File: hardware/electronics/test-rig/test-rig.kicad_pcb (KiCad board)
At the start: 2 copper layers, 154.8 x 27.9 mm, 57 parts, among them IC1 23LC1024, J1 JUMPER_OPEN, J2 JUMPER_CLOSED, J3 JUMPER_CLOSED, J4 AudioJack3_Switch, J5 Screw_Terminal_1x02, J6 Screw_Terminal_1x02, P1 CONN_01X15, P2 CONN_01X15, P3 CONN_01X04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

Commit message: WROOM and MEM layout completed
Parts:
- removed P8: CONN_01X06, Pin_Headers:Pin_Header_Straight_1x06_Pitch2.54mm
- moved R1 5.31 mm to (66.0, 111.5)
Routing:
- net /SI/IO23: track 34.1 -> 108.2 mm, vias 6 -> 4
- net /RAM-CS/IO22: track 12.2 -> 79.9 mm, vias 0 -> 2
- net +3V3: track 35.2 -> 92.7 mm
- net /SO/IO19: track 77.6 -> 126.1 mm
- net /XDCS/IO27: track 0.00 -> 48.0 mm, vias 0 -> 2
- net /IO14: track 0.00 -> 45.9 mm
- net /IO15: track 0.00 -> 43.6 mm, vias 0 -> 2
- net AGND: track 134.6 -> 170.9 mm, vias 11 -> 17
- net /IO13: track 0.00 -> 36.1 mm, vias 0 -> 2
- net /IO0: track 21.7 -> 54.7 mm, vias 1 -> 2
- net /EN: track 27.6 -> 56.8 mm
- net /TXD0: track 36.3 -> 26.3 mm
- net /RXDO: track 41.5 -> 31.5 mm
- net /SCK/IO18: track 75.6 -> 85.6 mm, vias 2 -> 3
- net /IO34: track 41.2 -> 43.7 mm
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
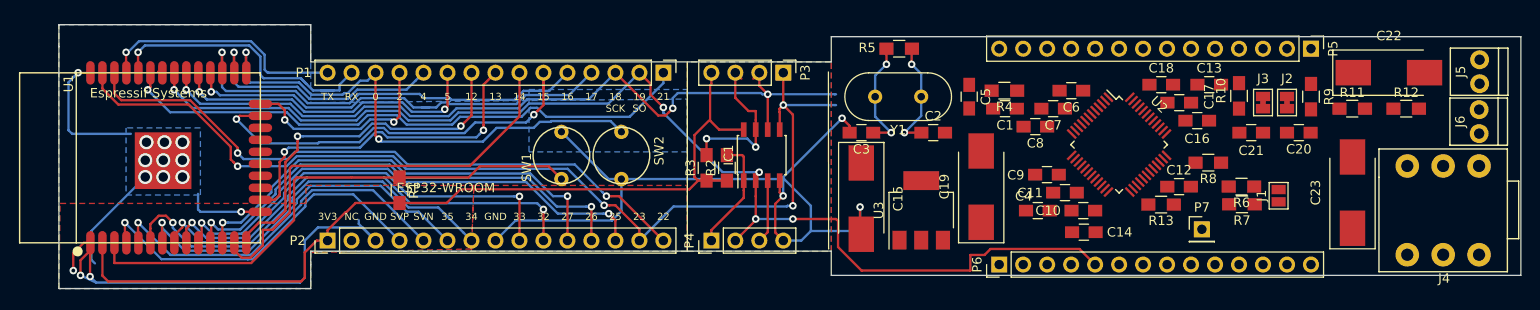
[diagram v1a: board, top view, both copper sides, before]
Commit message: New schematic
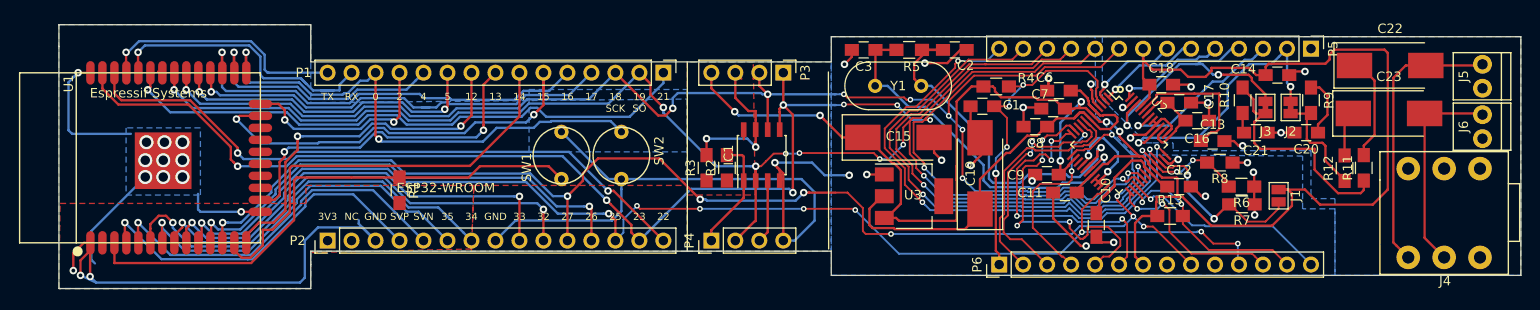
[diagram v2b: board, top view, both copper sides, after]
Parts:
- removed C4, C5: 10u, Capacitors_SMD:C_0805_HandSoldering
- removed P7: CONN_01X01, Pin_Headers:Pin_Header_Straight_1x01_Pitch2.54mm
- moved C14 26.4 mm to (159.0, 99.3), turned to 0 degrees
- moved C23 9.23 mm to (170.8, 103.4), turned to 0 degrees
- moved R12 9.07 mm to (166.1, 109.2), turned to 90 degrees
- moved C2 9.06 mm to (124.8, 96.6)
- moved C3 8.77 mm to (115.2, 96.6)
- moved C15 7.58 mm to (118.9, 105.9), turned to 0 degrees
- moved R11 6.39 mm to (168.1, 109.1), turned to 90 degrees
- moved C13 5.98 mm to (152.1, 106.3)
- moved C1 2.41 mm to (127.8, 102.6)
- moved C10 2.05 mm to (139.8, 115.2), turned to 270 degrees
- moved U3 1.68 mm to (120.5, 112.1), turned to 0 degrees
- moved R13 1.54 mm to (147.6, 114.2), turned to 0 degrees
- moved C19 1.40 mm to (127.5, 109.7)
- moved C6 1.31 mm to (135.9, 101.0)
- moved R8 1.22 mm to (152.9, 108.6)
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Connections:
- P5 pad 10: /GPIO2 -> /SI/IO23
- P5 pad 11: /GPIO1 -> /SO/IO19
- P5 pad 13: /MP3RST -> /GPIO1
- P5 pad 14: +3V3 -> /LROUT/GPIO4
- P5 pad 3: /LEFT -> /GBUF
- P5 pad 4: /GBUF -> /LEFT
- P5 pad 5: /MICP/LINE1 -> /LINE2
- P5 pad 6: /LINE2 -> /MICP/LINE1
- P5 pad 8: /VCO -> +3V3
- P5 pad 9: /GPIO3 -> /SCK/IO18
- P6 pad 1: +3V3 -> /MP3RST
- P6 pad 10: /SDATA/GPIO7 -> Net-(P6-Pad10)
- P6 pad 11: /SCLK/GPIO6 -> /XCS/IO25
- P6 pad 13: /LROUT/GPIO4 -> /RX
- P6 pad 14: AGND -> /TX
- P6 pad 2: /XDCS/IO27 -> /DREQ/IO26
- P6 pad 3: /DREQ/IO26 -> /GPIO2
- P6 pad 4: /XCS/IO25 -> /GPIO3
- P6 pad 5: /SO/IO19 -> /SCLK/GPIO6
- P6 pad 6: /SI/IO23 -> /SDATA/GPIO7
- P6 pad 7: /TX -> +3V3
- P6 pad 8: /RX -> AGND
- P6 pad 9: /SCK/IO18 -> /XDCS/IO27
- U2 pad 15: /VCO -> Net-(U2-Pad15)
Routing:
- net +3V3: track 92.7 -> 210.2 mm, vias 0 -> 6
- net /XDCS/IO27: track 48.0 -> 140.8 mm, vias 2 -> 9
- net /XCS/IO25: track 54.1 -> 134.0 mm, vias 2 -> 9
- net /GPIO1: track 0.00 -> 77.2 mm, vias 0 -> 4
- net /GPIO0: track 0.00 -> 68.4 mm, vias 0 -> 4
- net AGND: track 170.9 -> 239.1 mm, vias 17 -> 41
- net /SI/IO23: track 108.2 -> 173.7 mm, vias 4 -> 9
- net /SCK/IO18: track 85.6 -> 149.1 mm, vias 3 -> 9
- net +1.8V: track 0.00 -> 63.0 mm
- net /LROUT/GPIO4: track 0.00 -> 57.7 mm, vias 0 -> 3
- net /MP3RST: track 0.00 -> 35.9 mm, vias 0 -> 4
- net /SCLK/GPIO6: track 0.00 -> 33.8 mm, vias 0 -> 4
- net /SO/IO19: track 126.1 -> 159.2 mm, vias 5 -> 9
- net /SDATA/GPIO7: track 0.00 -> 31.0 mm, vias 0 -> 4
- net /RIGHT: track 0.00 -> 29.9 mm, vias 0 -> 2
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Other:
- net class D_Signal added: clearance 0.2, trace_width 0.2, via_dia 0.6, via_drill 0.3
- net class Power added: clearance 0.2, trace_width 0.25, via_dia 0.8, via_drill 0.4
